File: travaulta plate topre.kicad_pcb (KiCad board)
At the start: 4 copper layers, 209.7 x 76.4 mm, 54 parts

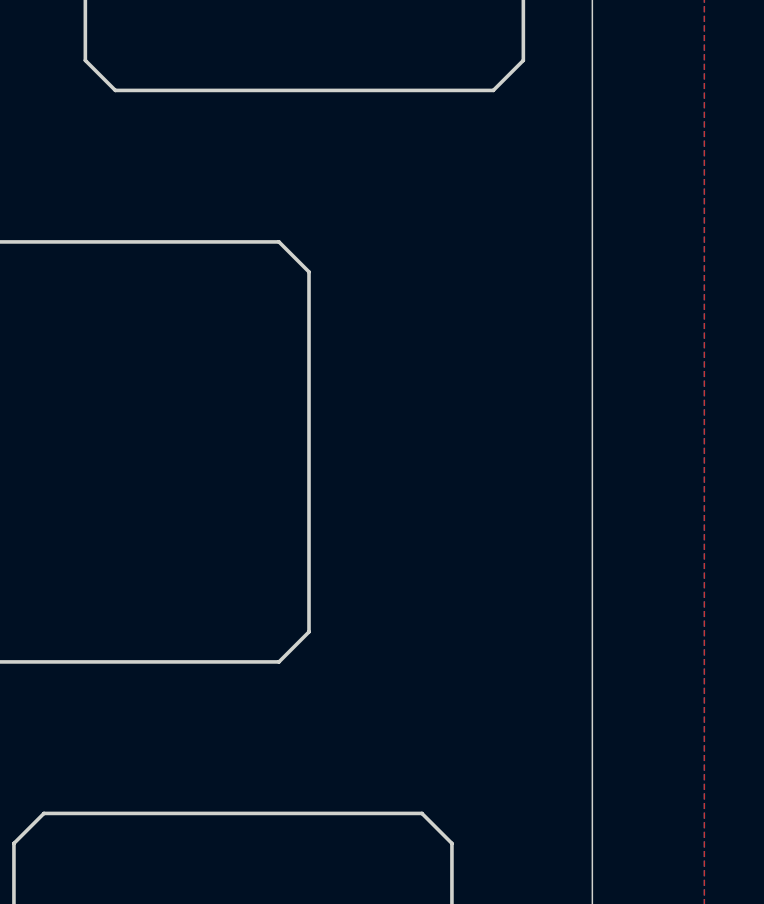
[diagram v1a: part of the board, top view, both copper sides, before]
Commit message: plate cutouts
needs plate edge cut
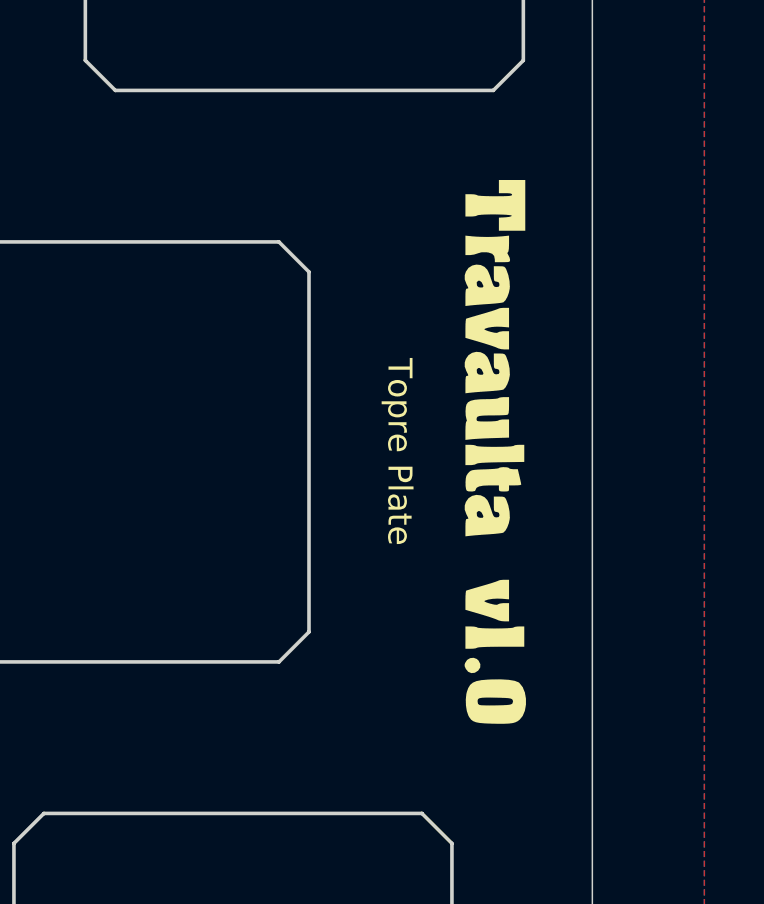
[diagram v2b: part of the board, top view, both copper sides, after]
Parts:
- added G***: LOGO, LOGO, F.Cu at (250.8, 76.2)
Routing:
- removed copper zone on In1.Cu, net GND
- removed copper zone on In2.Cu, net GND
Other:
- copper layers 4 -> 2
- board text added: "Topre Plate"

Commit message: first draft plates complete
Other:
- board size 209.7 x 76.4 mm -> 210.7 x 77.4 mm

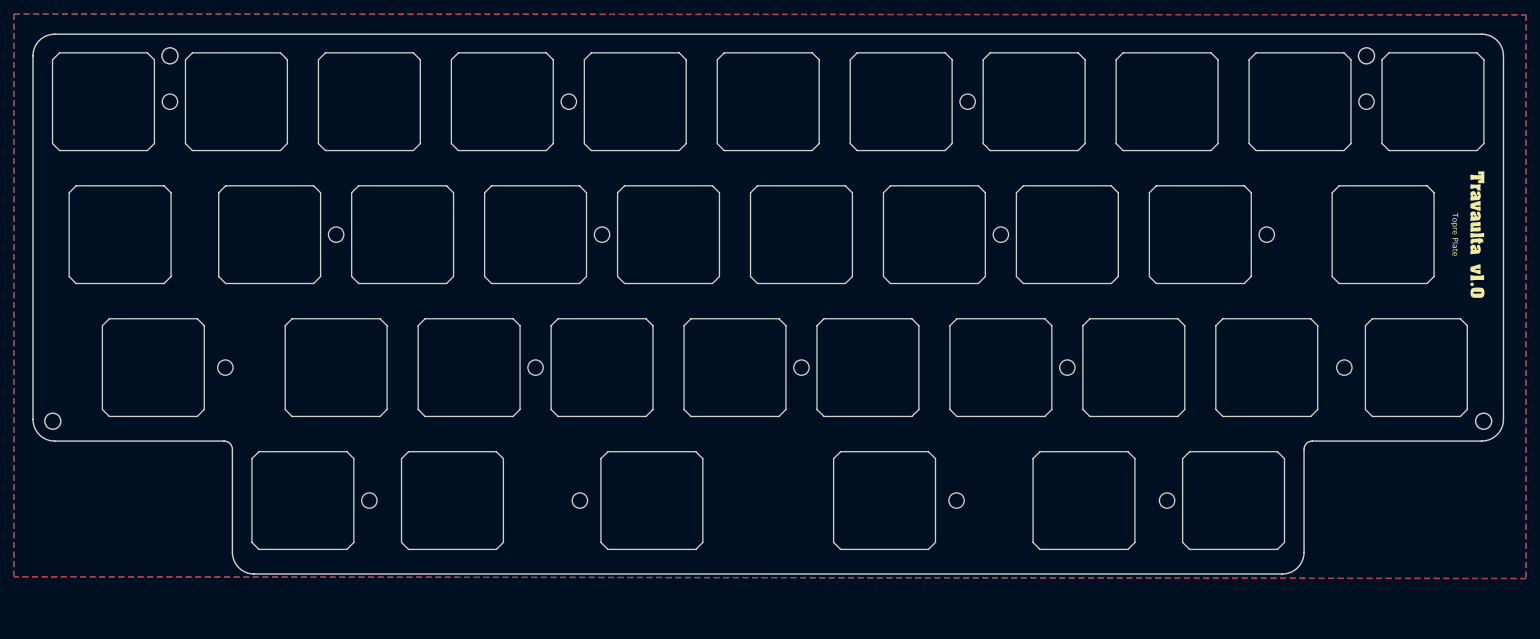
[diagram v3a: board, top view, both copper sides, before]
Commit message: edited preliminary firmware, small routing cleanups
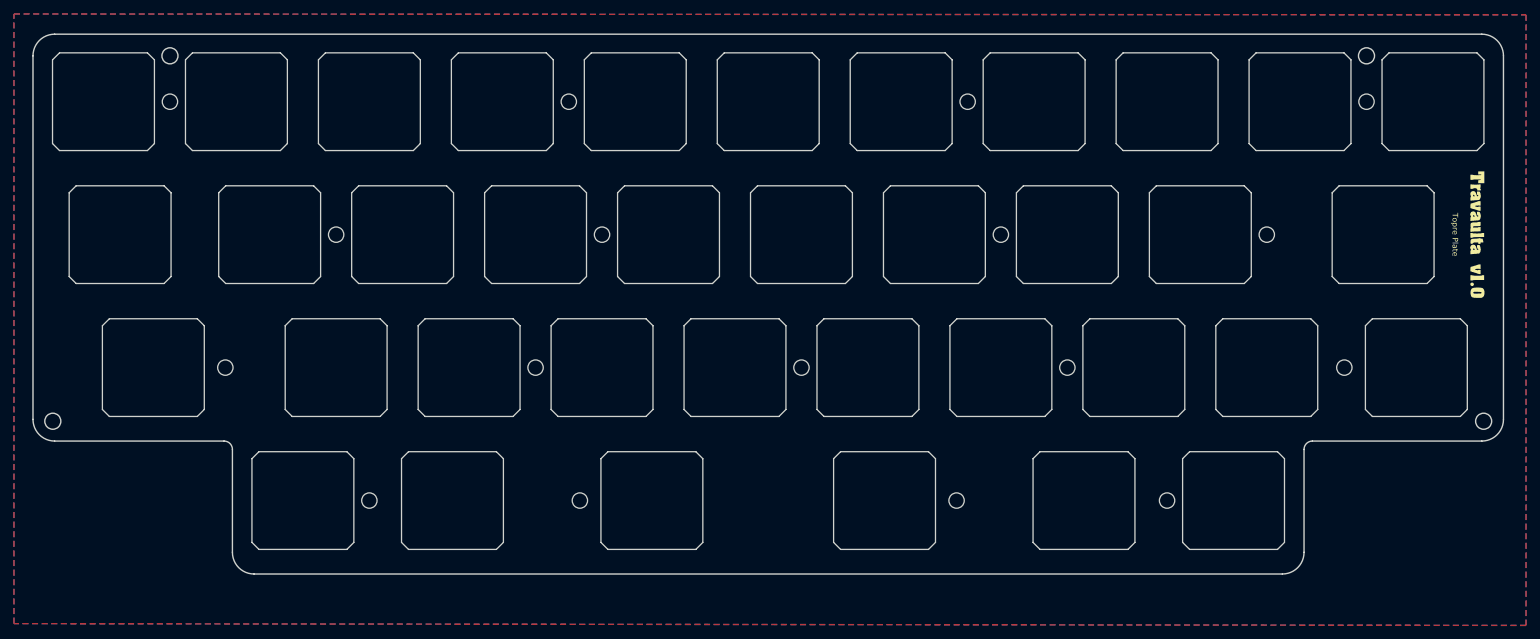
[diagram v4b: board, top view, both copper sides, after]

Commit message: fresh gerbers
deleted old plate gerbers, need new export
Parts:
- moved ? 0.79 mm to (175.4, 114.3)
- moved ? 0.79 mm to (70.6, 95.2)
- moved ? 0.79 mm to (123.0, 114.3)
- moved ? 0.79 mm to (232.6, 95.2)
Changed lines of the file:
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@@
   )
   (footprint "" (layer "F.Cu")
-    (at 176.2125 114.3)
+    (at 175.41875 114.3)
     (attr through_hole board_only)
     (fp_text reference "" (at 0 0) (layer "F.SilkS")
@@
   )
   (footprint "" (layer "F.Cu")
-    (at 71.4375 95.25)
+    (at 70.64375 95.25)
     (attr through_hole board_only)
     (fp_text reference "" (at 0 0) (layer "F.SilkS")
@@
   )
   (footprint "" (layer "F.Cu")
-    (at 122.2375 114.3)
+    (at 123.03125 114.3)
     (attr through_hole board_only)
     (fp_text reference "" (at 0 0) (layer "F.SilkS")
@@
   )
   (footprint "" (layer "F.Cu")
-    (at 231.775 95.25)
+    (at 232.56875 95.25)
     (attr through_hole board_only)
     (fp_text reference "" (at 0 0) (layer "F.SilkS")

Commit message: pcb clean up, fresh gerbers
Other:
- board text added: "JLCJLCJLCJLC"
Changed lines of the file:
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@@
   (gr_line (start 43.875 102.674999) (end 43.875 50.574999)
     (stroke (width 0.2) (type solid)) (layer "Edge.Cuts"))
+  (gr_text "JLCJLCJLCJLC" (at 249.2375 76.2 -90) (layer "B.SilkS")
+    (effects (font (size 1 1) (thickness 0.15)))
+  )
   (gr_text "Topre Plate" (at 247.65 76.2 270) (layer "F.SilkS")
     (effects (font (size 0.8 0.8) (thickness 0.15)))
